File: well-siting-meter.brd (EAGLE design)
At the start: 104.3 x 76.4 mm, 46 parts, among them J2 7805, T1 MOSFET-NCHANNELFQP30N06L, U1 LCD-16X2NOHOLES, U2 ARDUINO_PRO_MINI, U3 EC2, U4 EC2, U5 AD623, U6 AD623

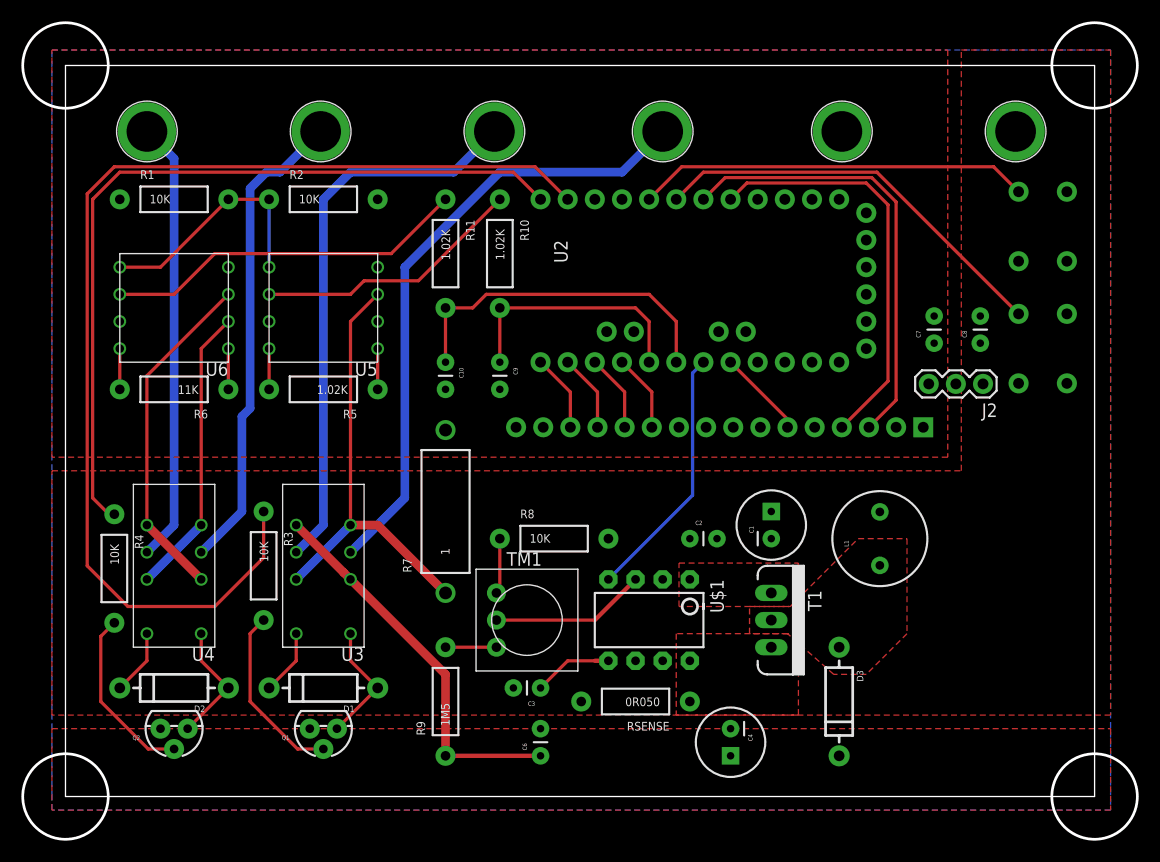
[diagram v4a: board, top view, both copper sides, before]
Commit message: updated inductor, adding part numbers
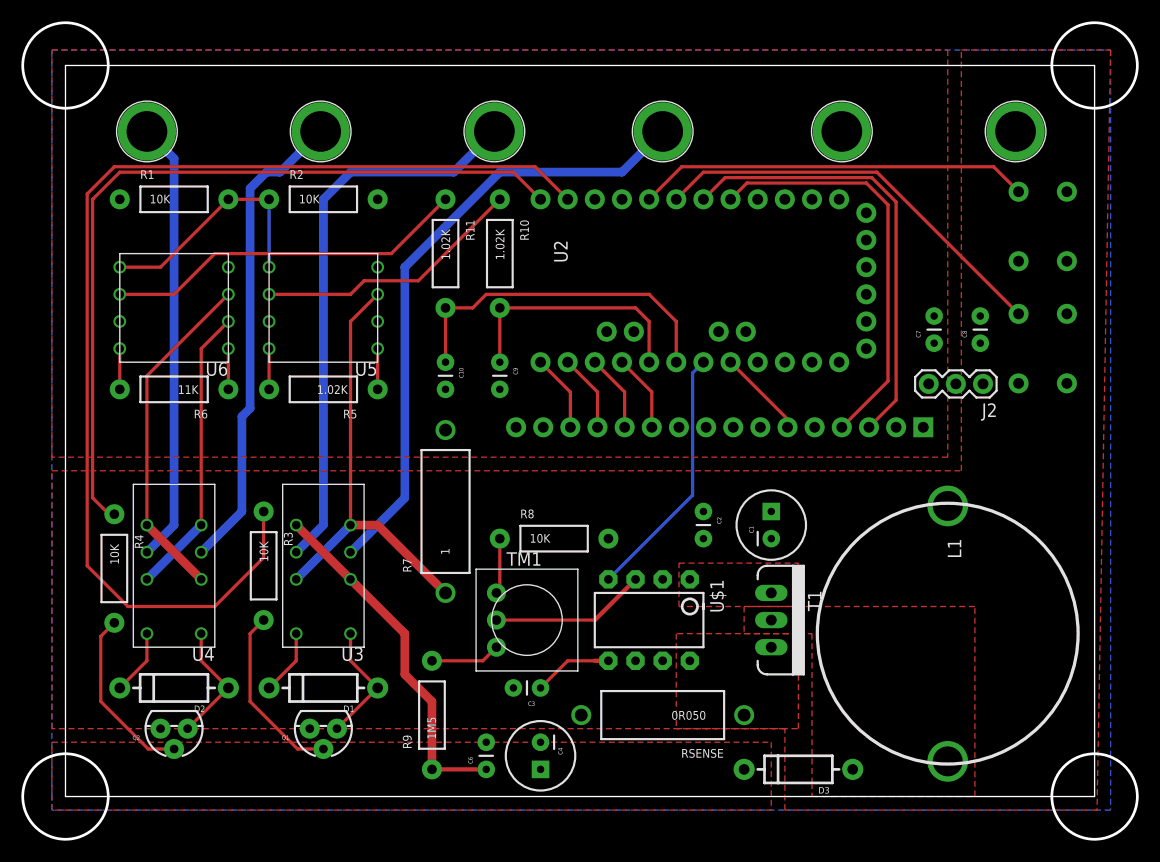
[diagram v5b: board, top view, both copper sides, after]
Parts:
- L1: value (none) -> MURATA1400; device SparkFun-Passives:RLB0912 -> murata1400:MURATA1400
- RSENSE: device SparkFun-Passives:AXIAL-0.4 -> SparkFun-Passives:AXIAL-0.6
- moved C4 17.8 mm to (44.5, 3.81)
- moved L1 10.9 mm to (82.5, 15.2), turned to 270 degrees
- moved D3 7.41 mm to (68.6, 2.54), turned to 180 degrees
- moved C6 5.24 mm to (39.4, 2.54)
- moved C2 2.84 mm to (59.7, 26.7), turned to 270 degrees
- moved RSENSE 2.84 mm to (55.9, 7.62)
- moved R9 1.80 mm to (34.3, 7.62)
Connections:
- net N$9: now also L1.P$2; no longer L1.2
- net V_BATT: now also L1.P$1; no longer L1.1
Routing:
- net VIN: track 36.3 -> 33.2 mm
- net N$6: track 4.76 -> 6.56 mm
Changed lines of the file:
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@@
 <element name="Q1" library="SparkFun-DiscreteSemi" package="TO-92" value="" x="24.13" y="6.35" rot="R180">
 <attribute name="PROD_ID" value="TRANS-09536" x="24.13" y="6.35" size="1.778" layer="27" rot="R180" display="off"/>
+<attribute name="PN" value="PN2222AFS-ND" x="24.13" y="6.35" size="1.778" layer="27" rot="R180" display="off"/>
 </element>
 <element name="Q2" library="SparkFun-DiscreteSemi" package="TO-92" value="" x="10.16" y="6.35" rot="R180">
 <attribute name="PROD_ID" value="TRANS-09536" x="10.16" y="6.35" size="1.778" layer="27" rot="R180" display="off"/>
-</element>
-<element name="D1" library="SparkFun-DiscreteSemi" package="DIODE-1N4001" value="" x="24.13" y="10.16" rot="R180"/>
-<element name="D2" library="SparkFun-DiscreteSemi" package="DIODE-1N4001" value="" x="10.16" y="10.16" rot="R180"/>
+<attribute name="PN" value="PN2222AFS-ND" x="10.16" y="6.35" size="1.778" layer="27" rot="R180" display="off"/>
+</element>
+<element name="D1" library="SparkFun-DiscreteSemi" package="DIODE-1N4001" value="" x="24.13" y="10.16" rot="R180">
+<attribute name="PN" value="1N4001FSCT-ND" x="24.13" y="10.16" size="1.778" layer="27" rot="R180" display="off"/>
+</element>
+<element name="D2" library="SparkFun-DiscreteSemi" package="DIODE-1N4001" value="" x="10.16" y="10.16" rot="R180">
+<attribute name="PN" value="1N4001FSCT-ND" x="10.16" y="10.16" size="1.778" layer="27" rot="R180" display="off"/>
+</element>
 <element name="R1" library="SparkFun-Passives" package="AXIAL-0.4" value="10K" x="10.16" y="55.88"/>
 <element name="R2" library="SparkFun-Passives" package="AXIAL-0.4" value="10K" x="24.13" y="55.88"/>
@@
 <element name="S1" library="SparkFun-Electromechanical" package="TACTILE-PTH" value="SWITCH-MOMENTARY-2PTH" x="91.44" y="41.91" rot="MR270">
 <attribute name="PROD_ID" value=" SWCH-08441" x="91.44" y="41.91" size="1.778" layer="28" rot="MR270" display="off"/>
+<attribute name="PN" value="SW406-ND" x="91.44" y="41.91" size="1.778" layer="28" rot="MR270" display="off"/>
 </element>
 <element name="S2" library="SparkFun-Electromechanical" package="TACTILE-PTH" value="SWITCH-MOMENTARY-2PTH" x="91.44" y="53.34" rot="MR270">
 <attribute name="PROD_ID" value=" SWCH-08441" x="91.44" y="53.34" size="1.778" layer="28" rot="MR270" display="off"/>
-</element>
-<element name="L1" library="SparkFun-Passives" package="RLB0912" value="" x="76.2" y="24.13" rot="R90"/>
+<attribute name="PN" value="SW406-ND" x="91.44" y="53.34" size="1.778" layer="28" rot="MR270" display="off"/>
+</element>
 <element name="C1" library="SparkFun-Passives" package="CPOL-RADIAL-100UF-25V" value="" x="66.04" y="25.4" rot="R90"/>
-<element name="C2" library="SparkFun-Passives" package="CAP-PTH-SMALL" value="" x="58.42" y="24.13"/>
+<element name="C2" library="SparkFun-Passives" package="CAP-PTH-SMALL" value="" x="59.69" y="26.67" rot="R270"/>
 <element name="C3" library="SparkFun-Passives" package="CAP-PTH-SMALL" value="" x="44.45" y="10.16" rot="R180"/>
 <element name="T1" library="SparkFun-DiscreteSemi" package="TO220V" value="MOSFET-NCHANNELFQP30N06L" x="66.04" y="16.51" rot="R270">
@@
 <attribute name="PN" value="FDP33N25-ND" x="66.04" y="16.51" size="1.778" layer="27" rot="R270" display="off"/>
 </element>
-<element name="D3" library="SparkFun-DiscreteSemi" package="DIODE-1N4001" value="" x="72.39" y="8.89" rot="R270">
-<attribute name="PN" value="EGP20FCT-ND" x="72.39" y="8.89" size="1.778" layer="27" rot="R270" display="off"/>
-</element>
-<element name="RSENSE" library="SparkFun-Passives" package="AXIAL-0.4" value="0R050" x="53.34" y="8.89" rot="R180"/>
+<element name="D3" library="SparkFun-DiscreteSemi" package="DIODE-1N4001" value="" x="68.58" y="2.54" rot="R180">
+<attribute name="PN" value="EGP20FCT-ND" x="68.58" y="2.54" size="1.778" layer="27" rot="R180" display="off"/>
+</element>
+<element name="RSENSE" library="SparkFun-Passives" package="AXIAL-0.6" value="0R050" x="55.88" y="7.62" rot="R180"/>
 <element name="R8" library="SparkFun-Passives" package="AXIAL-0.4" value="10K" x="45.72" y="24.13"/>
-<element name="R9" library="SparkFun-Passives" package="AXIAL-0.4" value="1M5" x="35.56" y="8.89" rot="R90"/>
-<element name="C6" library="SparkFun-Passives" package="CAP-PTH-SMALL" value="" x="44.45" y="3.81" rot="R90"/>
-<element name="C4" library="SparkFun-Passives" package="CPOL-RADIAL-100UF-25V" value="" x="62.23" y="5.08" rot="R270"/>
+<element name="R9" library="SparkFun-Passives" package="AXIAL-0.4" value="1M5" x="34.29" y="7.62" rot="R90"/>
+<element name="C6" library="SparkFun-Passives" package="CAP-PTH-SMALL" value="" x="39.37" y="2.54" rot="R90"/>
+<element name="C4" library="SparkFun-Passives" package="CPOL-RADIAL-100UF-25V" value="" x="44.45" y="3.81" rot="R270"/>
 <element name="U$1" library="max1771" package="DIP-08" value="MAX1771" x="54.61" y="16.51" rot="R180">
 <attribute name="PN" value="MAX1771CPA+-ND" x="54.61" y="16.51" size="1.778" layer="27" rot="R180" display="off"/>
@@
 <element name="C9" library="SparkFun-Passives" package="CAP-PTH-SMALL" value="" x="40.64" y="40.64" rot="R270"/>
 <element name="TM1" library="adafruit" package="TRIM-3386" value="" x="43.18" y="16.51" rot="R270"/>
+<element name="L1" library="murata1400" package="MURATA1400" value="MURATA1400" x="82.55" y="15.24" rot="R270">
+<attribute name="PN" value="811-2633-ND" x="82.55" y="15.24" size="1.778" layer="27" rot="R270" display="off"/>
+</element>
 </elements>
 <signals>
@@
 <contactref element="U3" pad="10"/>
 <contactref element="U3" pad="5"/>
-<wire x1="21.59" y1="25.4" x2="26.035" y2="20.955" width="0.8128" layer="1"/>
+<wire x1="21.59" y1="25.4" x2="26.67" y2="20.32" width="0.8128" layer="1"/>
 <contactref element="D3" pad="C"/>
 <contactref element="C4" pad="1"/>
 <contactref element="R9" pad="P$1"/>
 <contactref element="C6" pad="1"/>
-<wire x1="26.035" y1="20.955" x2="26.67" y2="20.32" width="0.8128" layer="1"/>
-<wire x1="44.45" y1="3.81" x2="35.56" y2="3.81" width="0.4064" layer="1"/>
+<wire x1="39.37" y1="2.54" x2="34.29" y2="2.54" width="0.4064" layer="1"/>
 <polygon width="0.3048" layer="1" rank="6">
 <vertex x="-1.27" y="-1.27"/>
-<vertex x="-1.27" y="6.35"/>
-<vertex x="97.79" y="6.35"/>
-<vertex x="97.79" y="-1.27"/>
-</polygon>
-<wire x1="35.56" y1="3.81" x2="35.56" y2="11.43" width="0.8128" layer="1"/>
-<wire x1="35.56" y1="11.43" x2="26.67" y2="20.32" width="0.8128" layer="1"/>
+<vertex x="-1.27" y="5.08"/>
+<vertex x="66.04" y="5.08"/>
+<vertex x="66.04" y="-1.27"/>
+</polygon>
+<wire x1="34.29" y1="2.54" x2="34.29" y2="8.89" width="0.8128" layer="1"/>
+<wire x1="34.29" y1="8.89" x2="31.75" y2="11.43" width="0.8128" layer="1"/>
+<wire x1="31.75" y1="11.43" x2="31.75" y2="15.24" width="0.8128" layer="1"/>
+<wire x1="31.75" y1="15.24" x2="26.67" y2="20.32" width="0.8128" layer="1"/>
 </signal>
 <signal name="V2">
@@
 <vertex x="83.82" y="69.85"/>
 <vertex x="97.79" y="69.85"/>
-<vertex x="97.79" y="7.62"/>
-<vertex x="-1.27" y="7.62"/>
+<vertex x="96.52" y="-1.27"/>
+<vertex x="67.31" y="-1.27"/>
+<vertex x="67.31" y="6.35"/>
+<vertex x="-1.27" y="6.35"/>
 </polygon>
 <contactref element="C1" pad="1"/>
+<contactref element="U$1" pad="2"/>
 <contactref element="C2" pad="1"/>
-<contactref element="L1" pad="1"/>
-<contactref element="U$1" pad="2"/>
+<contactref element="L1" pad="P$1"/>
 </signal>
 <signal name="RS">
@@
 </signal>
 <signal name="N$9">
-<contactref element="L1" pad="2"/>
 <contactref element="T1" pad="2"/>
 <contactref element="D3" pad="A"/>
-<polygon width="0.3048" layer="1" thermals="no" rank="2">
-<vertex x="64.008" y="17.78"/>
-<vertex x="67.818" y="17.78"/>
-<vertex x="74.168" y="24.13"/>
-<vertex x="78.74" y="24.13"/>
-<vertex x="78.74" y="15.24"/>
-<vertex x="74.93" y="11.43"/>
-<vertex x="71.882" y="11.43"/>
-<vertex x="67.564" y="15.24"/>
-<vertex x="64.008" y="15.24"/>
+<contactref element="L1" pad="P$2"/>
+<polygon width="0.3048" layer="1" thermals="no">
+<vertex x="63.5" y="15.24"/>
+<vertex x="68.58" y="15.24"/>
+<vertex x="69.85" y="15.24"/>
+<vertex x="69.85" y="1.27"/>
+<vertex x="69.85" y="0"/>
+<vertex x="85.09" y="0"/>
+<vertex x="85.09" y="17.78"/>
+<vertex x="63.5" y="17.78"/>
 </polygon>
 </signal>
@@
 <polygon width="0.3048" layer="1" thermals="no" rank="4">
 <vertex x="57.15" y="15.24"/>
-<vertex x="57.15" y="7.62"/>
-<vertex x="68.58" y="7.62"/>
+<vertex x="57.15" y="6.35"/>
+<vertex x="68.58" y="6.35"/>
 <vertex x="68.58" y="15.24"/>
 </polygon>
@@
 <contactref element="R9" pad="P$2"/>
 <contactref element="TM1" pad="3"/>
-<wire x1="35.56" y1="13.97" x2="40.3225" y2="13.97" width="0.3048" layer="1"/>
+<wire x1="34.29" y1="12.7" x2="39.0525" y2="12.7" width="0.3048" layer="1"/>
+<wire x1="39.0525" y1="12.7" x2="40.3225" y2="13.97" width="0.3048" layer="1"/>
 </signal>
 <signal name="N$8">

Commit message: fixed board outline, added remaining part numbers
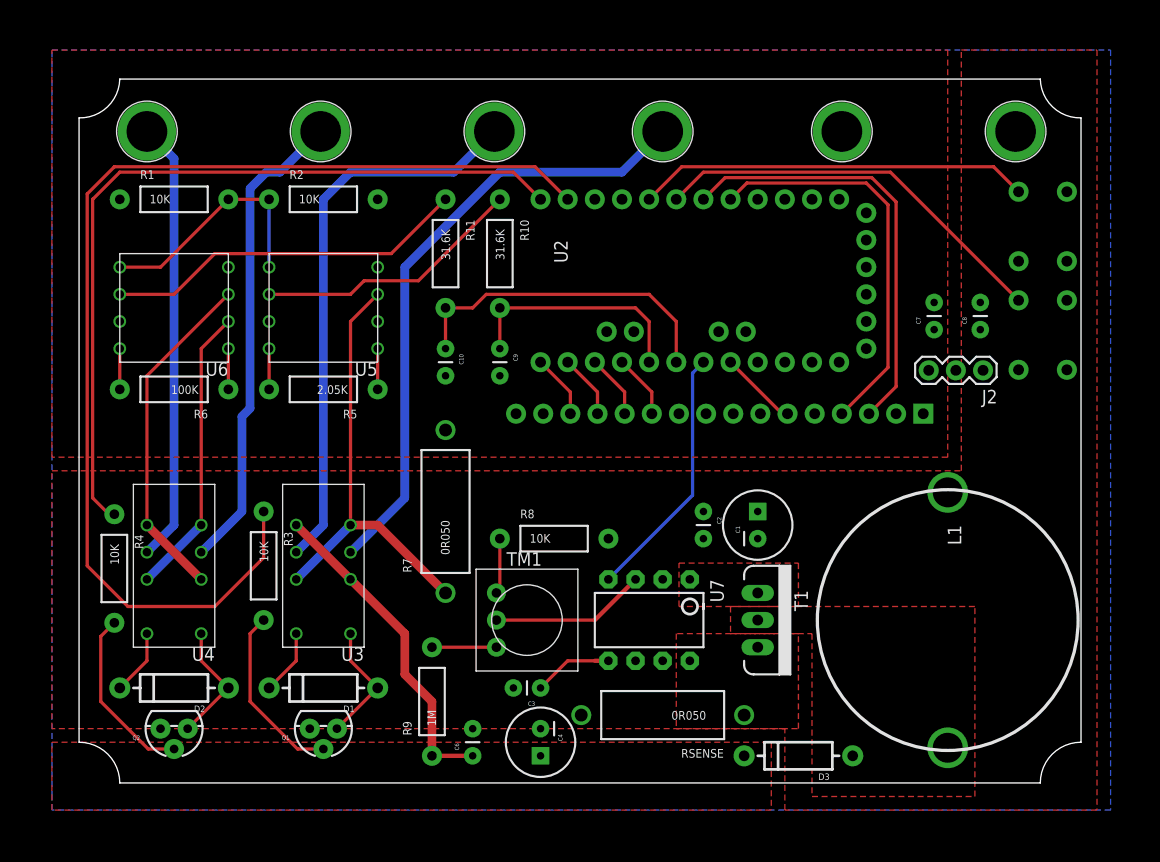
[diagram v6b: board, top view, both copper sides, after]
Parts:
- C1: value (none) -> 100uF, 35V
- C10, C2, C3, C9: value (none) -> 0.1uf
- C4: value (none) -> 4u7, 250V
- C6: value (none) -> 0.1uf, 250V
- R10, R11: value 1.02K -> 31.6K
- R5: value 1.02K -> 2.05K
- R6: value 11K -> 100K
- R7: value 1 -> 0R050
- R9: value 1M5 -> 1M
- moved C6 1.80 mm to (38.1, 3.81)
- moved C1 1.27 mm to (64.8, 25.4)
- moved T1 1.27 mm to (64.8, 16.5)
- moved C7 1.27 mm to (81.3, 43.7)
- moved C8 1.27 mm to (85.6, 43.7)
- moved J2 1.27 mm to (85.9, 39.9)
- moved S1 1.27 mm to (91.4, 43.2)
- moved L1 1.27 mm to (82.5, 16.5)
- moved R9 1.27 mm to (34.3, 8.89)
- moved C4 1.27 mm to (44.5, 5.08)
- moved D3 1.27 mm to (68.6, 3.81)
- moved U1 1.27 mm to (48.3, 20.3)
- moved C10 1.27 mm to (35.6, 41.9)
- moved C9 1.27 mm to (40.6, 41.9)
- renumbered U$1 to U7
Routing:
- net VIN: track 33.2 -> 30.7 mm
- net VO: track 41.9 -> 40.7 mm
- net RS: track 38.8 -> 37.5 mm
- net DB7: track 7.25 -> 5.98 mm
- net DB6: track 7.25 -> 5.98 mm
- net DB5: track 7.25 -> 5.98 mm
- net DB4: track 7.25 -> 5.98 mm
- net VOUT: track 32.1 -> 30.8 mm
- net IOUT: track 23.4 -> 22.1 mm
- net E: track 8.30 -> 7.33 mm
- net N$6: track 6.56 -> 6.03 mm
- net B1: track 38.6 -> 38.0 mm
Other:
- board size 104.3 x 76.4 mm -> 93.8 x 65.9 mm
